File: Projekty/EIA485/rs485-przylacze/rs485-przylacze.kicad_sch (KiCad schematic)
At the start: 16 parts, among them U1 MAX3485, U2 MAX3485

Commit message: Schemat elektryczny EIA485 v0.3
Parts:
- removed D1: 304YD2J-1B, symbol Device:LED
- removed D2: FYL-3014D1A, symbol Device:LED
- removed M?: MPMOS, symbol pspice:MPMOS
- removed M?: MNMOS, symbol pspice:MNMOS
- removed R4: 110, symbol Device:R
- added C2, C4: 10 uF, symbol Device:C_Polarized
- added C5, C6: 0.1 uF, symbol pspice:C
- added D3: L-7113LYD, symbol Device:LED
- added D4: LTL-307ELC, symbol Device:LED
- added J1: OUTPUT, symbol Connector_Generic:Conn_01x04
- added J2: INPUT, symbol Connector_Generic:Conn_01x06
- added Q1, Q2: 2N7002, Package_TO_SOT_SMD:SOT-23, symbol Transistor_FET:2N7002
- added R1, R10, R11, R12, R13, R14, R15, R2: 10k, symbol Device:R
- added R6, R7: 750, symbol Device:R
- added R8, R9: 300, symbol Device:R
- added RT3: 62, symbol Device:R
- added U3: NL27WZ08USG, ON_Semiconductor-493-09_2021-F-*, symbol NL27WZ08USG:NL27WZ08USG
- added U4: 74AHC1G04, symbol 74xGxx:74AHC1G04
- R3: value 110 -> 10k
- RT2: value 120 -> 62
- gave numbers to parts that had none: 1
- renumbered C2 to C3, D4 to D2, R2 to R4, R3 to R5
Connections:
- net +3V3: now also R3.1, C2.1, C4.1, R12.1, R13.1, R2.1, R6.1, R7.1
- net A: now also J1.3 (Pin_3), RT3.2; no longer RT2.2
- net B: now also J1.2 (Pin_2)
- net GND: now also C2.2, C4.2, C5.2, C6.2, J1.1 (Pin_1), J2.6 (Pin_6), Q1.2 (S), Q2.2 (S), R1.2, R10.1, R11.2, R14.1, R15.2, U3.4 (GND), U4.3 (GND)
- net RX_MCU: now also R3.2, J2.4 (Pin_4), R13.2
- net TX_MCU: now also J2.5 (Pin_5), R12.2, R2.2
- net ENABLE_DISABLE renamed RX/TX ENABLE
- net RX/TX ENABLE: now also R1.1, R11.1
- new net: D4.2 (A), R7.2
- new net: R10.2, R8.1, U3.7 (Y1)
- new net: D4.1 (K), Q2.3 (D)
- new net: RT2.2, RT3.1
- new net: Q1.1 (G), R8.2
- new net: D3.1 (K), Q1.3 (D)
- new net: D3.2 (A), R6.2
- new net: R14.2, R9.1, U3.3 (Y2)
- new net: U3.6 (B2), U4.4
- new net: Q2.1 (G), R9.2
- new net +12V: J1.4 (Pin_4), J2.1 (Pin_1)
- new net +5V: C5.1, C6.1, U3.8 (VCC), U4.5 (VCC)
- new net RX/TX ENABLE : J2.3 (Pin_3), U3.2 (B1), U4.2
- new net RX/TX SWITCH: J2.2 (Pin_2), R15.1, U3.1 (A1), U3.5 (A2)
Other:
- note added: "D3 - wysoki stan logiczny, kolor żółty D4 - niski stan logiczny, kolor czerwony"
- note removed: "D1 - wysoki stan logiczny, kolor żółty D2 - niski stan logiczny, kolor czerwony"
- moved on the sheet: C1, C3, D2, RT2

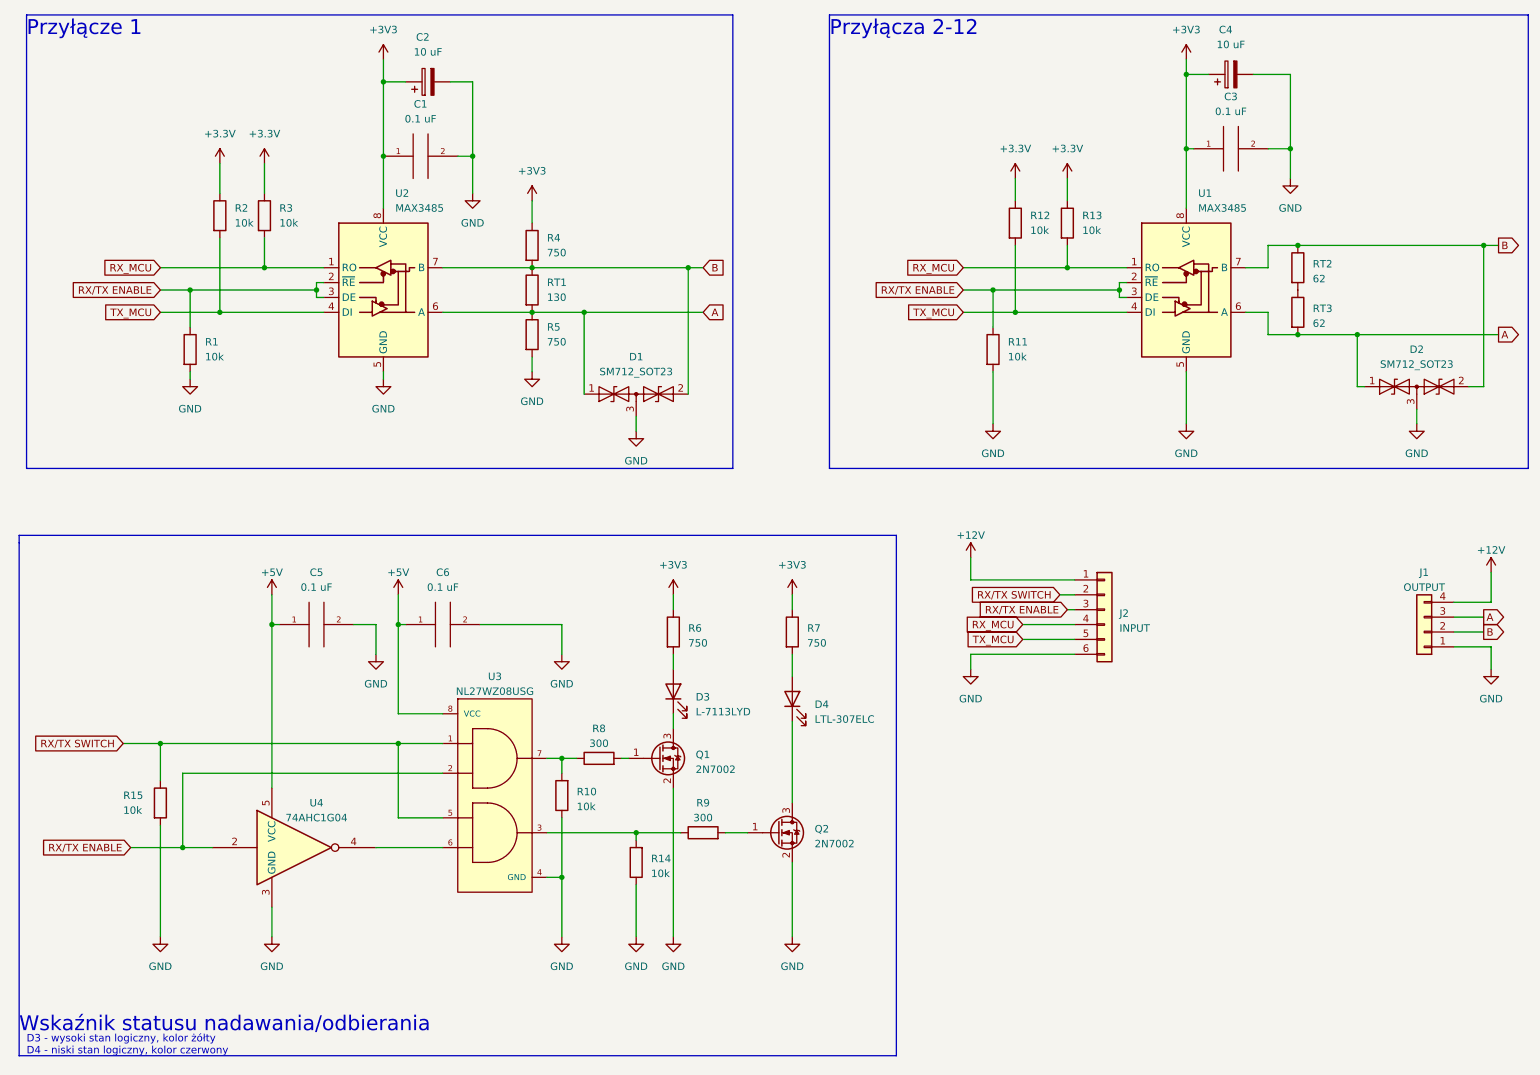
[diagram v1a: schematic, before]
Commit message: Schemat elektryczny EIA485 v0.4
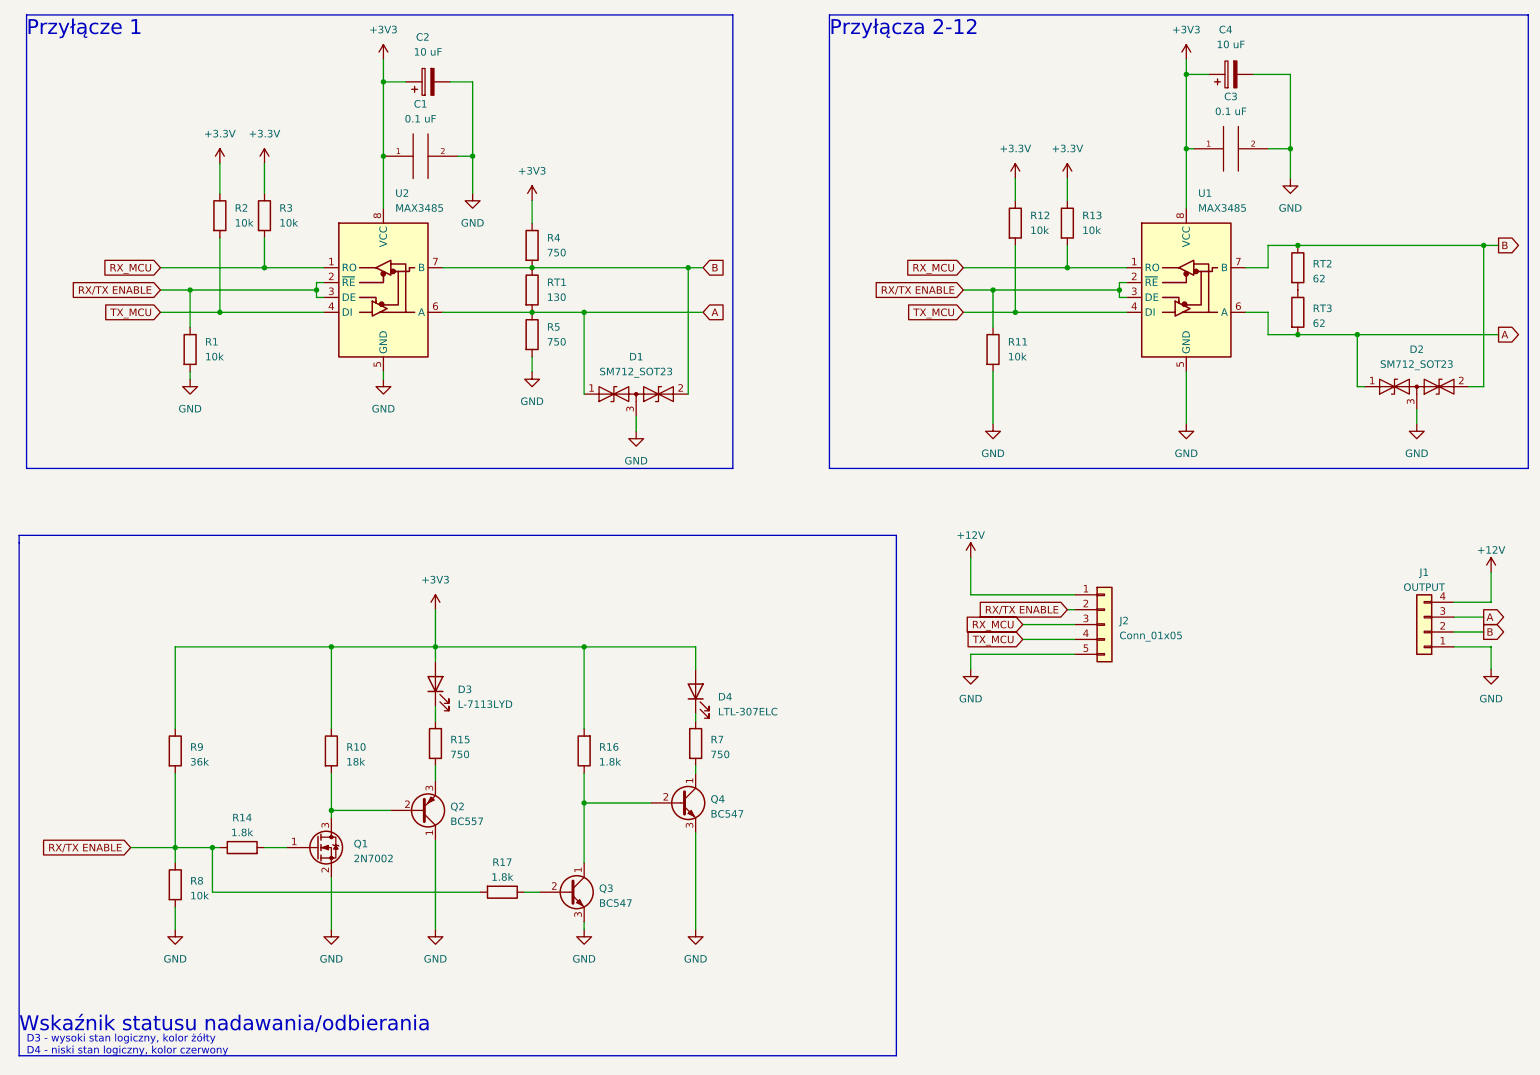
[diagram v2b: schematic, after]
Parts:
- removed C5, C6: 0.1 uF, symbol pspice:C
- removed J2: INPUT, symbol Connector_Generic:Conn_01x06
- removed Q2: 2N7002, Package_TO_SOT_SMD:SOT-23, symbol Transistor_FET:2N7002
- removed R6: 750, symbol Device:R
- removed U3: NL27WZ08USG, ON_Semiconductor-493-09_2021-F-*, symbol NL27WZ08USG:NL27WZ08USG
- removed U4: 74AHC1G04, symbol 74xGxx:74AHC1G04
- added J2: Conn_01x05, symbol Connector_Generic:Conn_01x05
- added Q2: BC557, Package_TO_SOT_THT:TO-92_Inline, symbol Transistor_BJT:BC557
- added Q3, Q4: BC547, Package_TO_SOT_THT:TO-92_Inline, symbol Transistor_BJT:BC547
- added R16, R17: 1.8k, Resistor_THT:R_Axial_DIN0207_L6.3mm_D2.5mm_P7.62mm_Horizontal, symbol Device:R
- C1, C3: footprint (none) -> Capacitor_THT:C_Disc_D3.0mm_W1.6mm_P2.50mm
- C2, C4: footprint (none) -> Capacitor_THT:CP_Radial_Tantal_D10.5mm_P5.00mm
- R1, R11, R12, R13, R2, R3, R4, R5, R7, RT2, RT3: footprint (none) -> Resistor_THT:R_Axial_DIN0207_L6.3mm_D2.5mm_P7.62mm_Horizontal
- R10: value 10k -> 18k; footprint (none) -> Resistor_THT:R_Axial_DIN0207_L6.3mm_D2.5mm_P7.62mm_Horizontal
- R14: value 10k -> 1.8k; footprint (none) -> Resistor_THT:R_Axial_DIN0207_L6.3mm_D2.5mm_P7.62mm_Horizontal
- R15: value 10k -> 750; footprint (none) -> Resistor_THT:R_Axial_DIN0207_L6.3mm_D2.5mm_P7.62mm_Horizontal
- R8: value 300 -> 10k; footprint (none) -> Resistor_THT:R_Axial_DIN0207_L6.3mm_D2.5mm_P7.62mm_Horizontal
- R9: value 300 -> 36k; footprint (none) -> Resistor_THT:R_Axial_DIN0207_L6.3mm_D2.5mm_P7.62mm_Horizontal
- RT1: footprint (none) -> Resistor_THT:R_Axial_DIN0207_L6.3mm_D2.5mm_P5.08mm_Vertical
- U1, U2: footprint (none) -> Package_SO:SO-8_3.9x4.9mm_P1.27mm
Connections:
- net RX/TX SWITCH is gone; now on an unnamed net: R15.1
- net +12V: now also J2.1 (Pin_1)
- net +3V3: now also D3.2 (A), D4.2 (A), R10.1, R9.1, R16.2; no longer R7.1
- net GND: now also R8.2, J2.5 (Pin_5), Q2.1 (C), Q3.3 (E), Q4.3 (E); no longer R10.1, R14.1, R15.2
- net RX_MCU: now also J2.3 (Pin_3)
- net RX/TX ENABLE : now also R14.1, R8.1, R9.2, J2.2 (Pin_2), R17.2
- net TX_MCU: now also J2.4 (Pin_4)
- net at R7.2: now also Q4.1 (C); no longer D4.2 (A)
- net at R10.2: now also Q1.3 (D), Q2.2 (B); no longer R8.1
- net at D4.1 (K): now also R7.1
- net at Q1.1 (G): now also R14.2; no longer R8.2
- net at D3.1 (K): no longer Q1.3 (D)
- new net: Q3.1 (C), Q4.2 (B), R16.1
- new net: Q2.3 (E), R15.2
- new net: Q3.2 (B), R17.1
